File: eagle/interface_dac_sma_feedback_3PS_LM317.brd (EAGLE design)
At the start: 95.6 x 144.9 mm, 37 parts, among them IC1 ISO1540, IC2 LT1352PA, IC3 LT1352PA, X1 BU-SMA-V

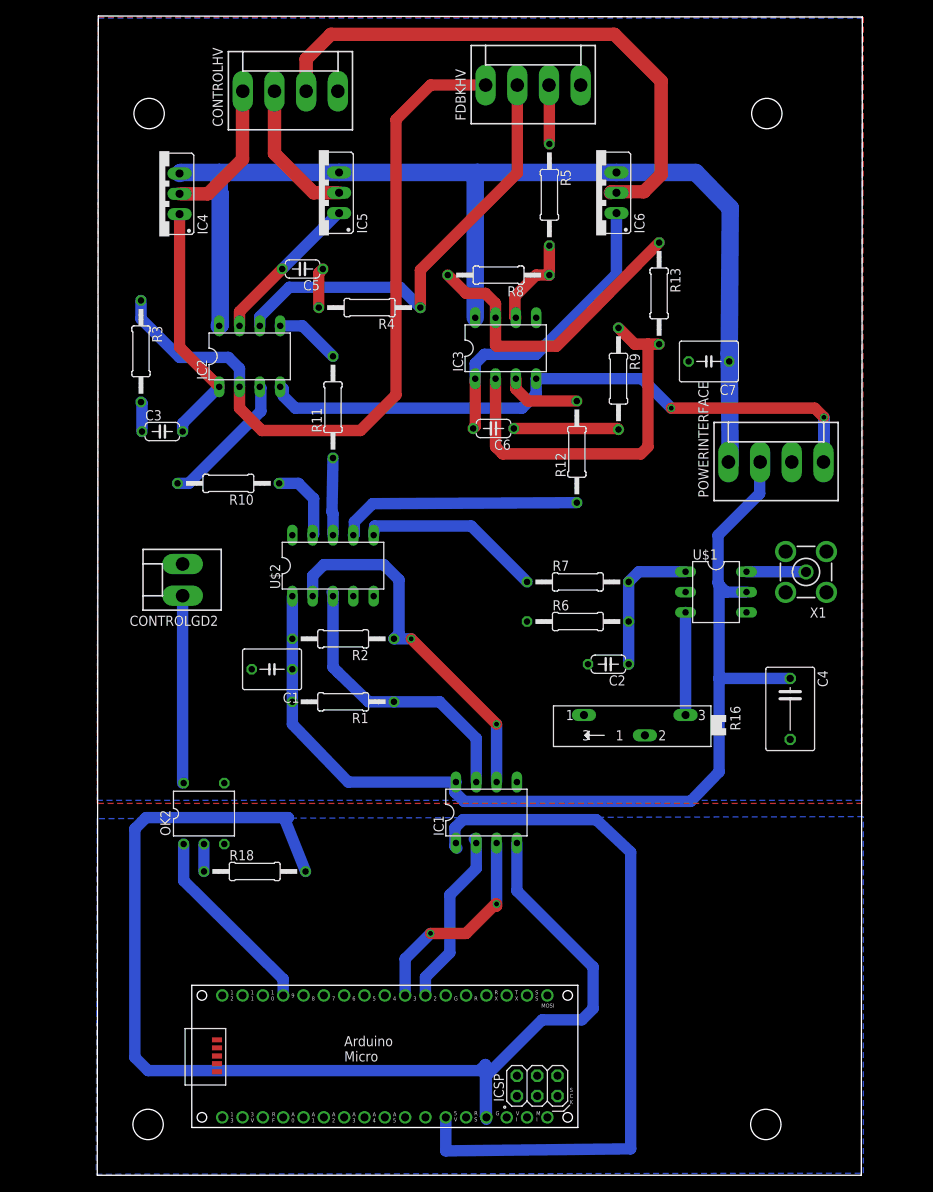
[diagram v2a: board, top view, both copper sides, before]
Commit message: optional 317 regulation of emcos
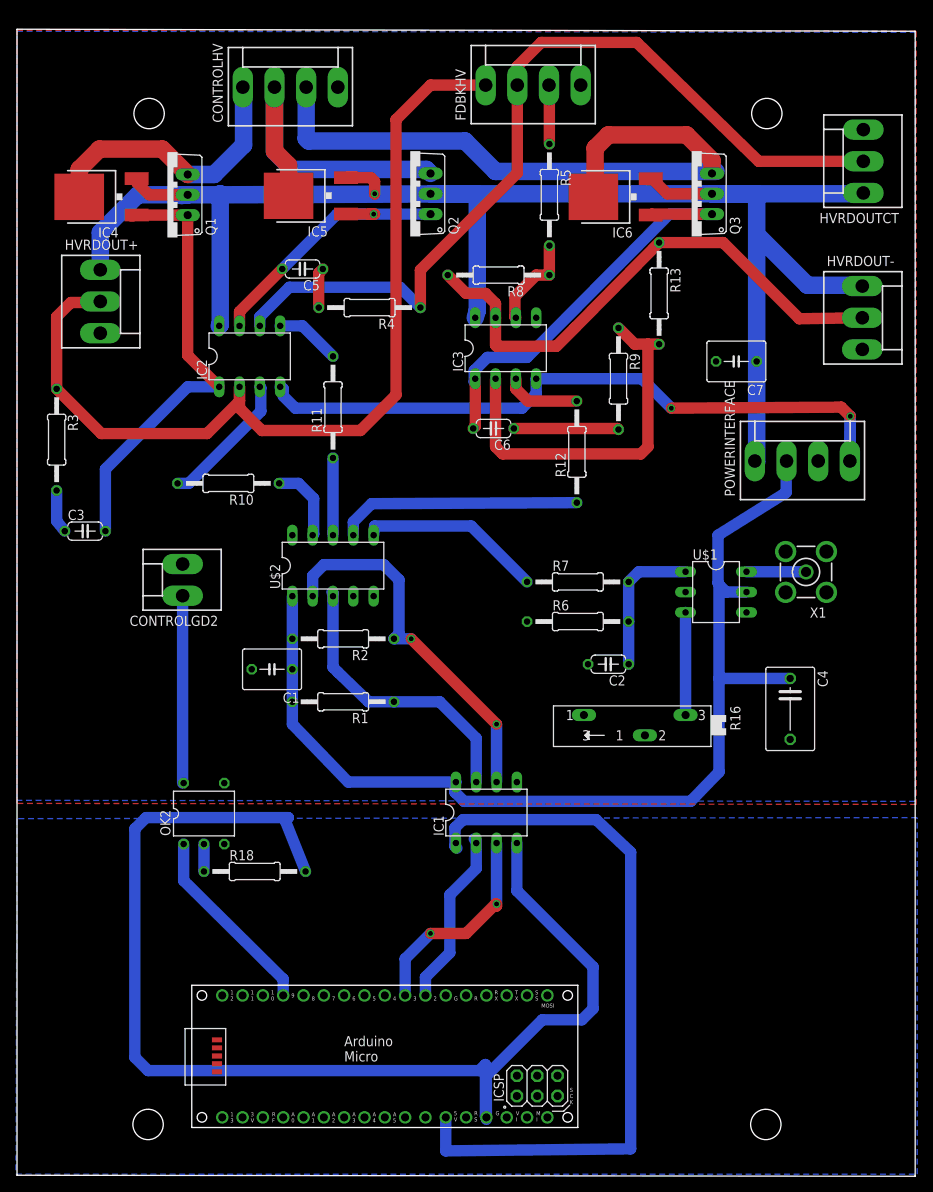
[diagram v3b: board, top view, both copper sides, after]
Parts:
- added HVRDOUT+, HVRDOUT-, HVRDOUTCT: (no value), con-molex:KK-156-3
- added Q1, Q2, Q3: TIP122V, transistor-npn:TO220V
- IC4, IC5, IC6: value (none) -> LM317MABDT; device v-reg:317TS -> v-reg:DPACK
- R12: value 12 -> 10k
- moved C3 15.8 mm to (-1.52, 80.5)
- moved R3 15.3 mm to (-5.08, 91.9)
- moved IC4 7.63 mm to (0.13, 122.3)
- moved C7 3.43 mm to (79.9, 101.7)
- moved POWERINTERFACE 3.30 mm to (88.1, 89.3)
- moved IC6 2.09 mm to (64.4, 122.3)
- moved IC5 1.45 mm to (26.3, 122.4)
- moved CONTROLHV 0.51 mm to (24.1, 136.0)
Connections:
- net +12V: now also HVRDOUT+.1, HVRDOUT-.1, HVRDOUTCT.1, Q1.2, Q2.2, Q3.2
- net GND: now also HVRDOUT+.3, HVRDOUT-.3, HVRDOUTCT.3
- net N$10: now also Q2.1
- net N$11: now also CONTROLHV.2, IC5.4, Q2.3; no longer CONTROLHV.3, IC6.2
- net N$14: now also HVRDOUT-.2
- net N$19: now also Q1.1
- net N$21: now also Q3.1
- net N$4: now also IC4.4, Q1.3; no longer IC4.2
- net N$5: now also CONTROLHV.3, IC6.4, Q3.3; no longer CONTROLHV.2, IC5.2
- net N$6: now also HVRDOUTCT.2
- net N$8: now also HVRDOUT+.2
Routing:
- net +12V: track 140.7 -> 219.3 mm, vias 0 -> 1
- net N$5: track 17.9 -> 83.2 mm
- net N$6: track 56.6 -> 109.5 mm
- net N$14: track 38.6 -> 67.9 mm
- net N$11: track 71.1 -> 43.0 mm
- net N$19: track 31.1 -> 56.4 mm
- net N$8: track 92.1 -> 116.5 mm
- net N$4: track 18.5 -> 35.2 mm
- net N$10: track 19.0 -> 35.0 mm, vias 0 -> 1
- net N$21: track 38.6 -> 53.5 mm
- net -5V: track 85.4 -> 88.7 mm
- net VCC: track 130.4 -> 133.1 mm
- net N$3: track 3.74 -> 5.44 mm
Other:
- board size 95.6 x 144.9 mm -> 112.3 x 143.4 mm
